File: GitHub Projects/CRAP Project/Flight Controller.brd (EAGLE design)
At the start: 40 x 93 mm, 126 parts, among them J1 2POS_SCREWTERM, J101 2POS_SCREWTERM, J2 4POS_SCREWTERM, J3 4POS_SCREWTERM, J4 4POS_SCREWTERM, J5 4POS_SCREWTERM, Q101 IPD042P03L3G, Q102 IPD042P03L3G, Q1101 PMF170XP, Q1102 DMG4800LSD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

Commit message: Routing, schematic changes
1. Changed some schematic errors on the firing chains
2. Routed more GPS, changed inductor on power supply, routed Xbee
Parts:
- L801, L802: device rcl:L1812 -> rcl:R0805
- moved C805 499.3 mm to (30.0, 97.0)
- moved L804 499.3 mm to (12.0, 102.0)
- moved L803 494.5 mm to (23.0, 96.0), turned to 180 degrees
- moved L801 480.2 mm to (30.0, 89.0), turned to 270 degrees
- moved L802 476.2 mm to (10.0, 89.0), turned to 270 degrees
- moved C803 469.5 mm to (29.0, 81.0), turned to 90 degrees
- moved C804 469.5 mm to (29.0, 77.0), turned to 90 degrees
- moved C802 467.5 mm to (26.0, 84.0), turned to 315 degrees
- moved C801 460.8 mm to (15.0, 85.0)
- moved J5 197.6 mm to (34.0, 39.5), turned to 90 degrees
- moved C2 175.6 mm to (21.0, 44.0), flipped to the bottom, turned to 135 degrees
- moved C1 172.2 mm to (19.0, 46.0), flipped to the bottom, turned to 45 degrees
- moved C3 167.8 mm to (17.6, 49.1), flipped to the bottom, turned to 135 degrees
- moved L101 4.12 mm to (27.0, 40.0), flipped to the bottom
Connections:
- removed net FC2+: J3.3
- removed net FC4+: J4.3
- removed net GPS1:+3V3: C803.2, C804.2, U$801.8
- net +12V: now also J3.3, J4.3
- net +3V3: now also C803.2, C804.2, U$801.8
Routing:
- net +3V3: track 75.0 -> 252.1 mm, vias 4 -> 8
- net VDDOUT: track 0.00 -> 24.9 mm, vias 0 -> 3
- net GPS1:N$2: track 0.00 -> 17.7 mm, vias 0 -> 1
- net GPS1:N$3: track 0.00 -> 12.6 mm, vias 0 -> 1
- net DCDC_REGULATOR:N$3: track 6.94 -> 9.19 mm, vias 0 -> 1
- net DCDC_REGULATOR:N$5: track 13.2 -> 14.7 mm, vias 0 -> 1
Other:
- board text added: "BW_1"
- board text added: "BW_2"

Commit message: More routing changes
1. Changed the power circuit 180 degrees to better fit the inductor
2. Routed a lot of the ordance circuits and placed all MOSFETS
3. Routed lots of power
4. Oh god it's so crowded
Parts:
- moved Q1102 402.9 mm to (28.6, 68.1), flipped to the bottom, turned to 180 degrees
- moved Q1202 342.6 mm to (27.0, 60.0), flipped to the bottom, turned to 90 degrees
- moved Q1302 287.1 mm to (27.0, 54.0), flipped to the bottom, turned to 90 degrees
- moved C307 263.2 mm to (10.2, 54.9), flipped to the bottom, turned to 270 degrees
- moved C306 261.8 mm to (9.22, 60.0), flipped to the bottom, turned to 270 degrees
- moved U301 130.2 mm to (4.61, 59.3), flipped to the bottom
- moved D301 120.1 mm to (18.3, 72.3), flipped to the bottom
- moved L101 18.1 mm to (9.00, 38.0), flipped to the top
- moved C103 9.79 mm to (23.7, 35.5), turned to 180 degrees
- moved U$101 9.00 mm to (15.0, 33.0), turned to 180 degrees
- moved C102 7.64 mm to (23.2, 32.3), turned to 90 degrees
- moved C804 3.36 mm to (28.5, 80.3), turned to 0 degrees
- moved R102 3.30 mm to (16.8, 63.8)
- moved R106 3.27 mm to (20.9, 32.2), turned to 270 degrees
- moved C101 2.22 mm to (18.7, 32.2), turned to 90 degrees
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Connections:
- removed net FC3-: J4.2
- net FC1-2: now also J4.2
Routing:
- net DCDC_REGULATOR:VIN: track 18.9 -> 72.1 mm
- net ORDNANCE_POWER:N$3: track 0.00 -> 28.6 mm, vias 0 -> 1
- net ORDNANCE_POWER:N$7: track 0.00 -> 11.1 mm
- net FC1-3: track 0.00 -> 10.5 mm
- net DCDC_REGULATOR:N$5: track 14.7 -> 6.54 mm, vias 1 -> 0
- net FC1-2: track 0.00 -> 7.50 mm
- net FC1-1: track 0.00 -> 7.35 mm
- net VCC_IN: track 29.9 -> 25.9 mm
- net DCDC_REGULATOR:N$3: track 9.19 -> 12.7 mm, vias 1 -> 0
- net DCDC_REGULATOR:N$6: track 35.8 -> 39.1 mm, vias 0 -> 2
- net FC1-: track 4.80 -> 7.73 mm
- net +3V3: track 252.1 -> 254.0 mm
- net DCDC_REGULATOR:N$2: track 22.8 -> 21.3 mm
- net DCDC_REGULATOR:N$4: track 9.78 -> 11.1 mm
- net DCDC_REGULATOR:N$11: track 8.65 -> 7.93 mm
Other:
- board size 40 x 93 mm -> 40 x 95 mm

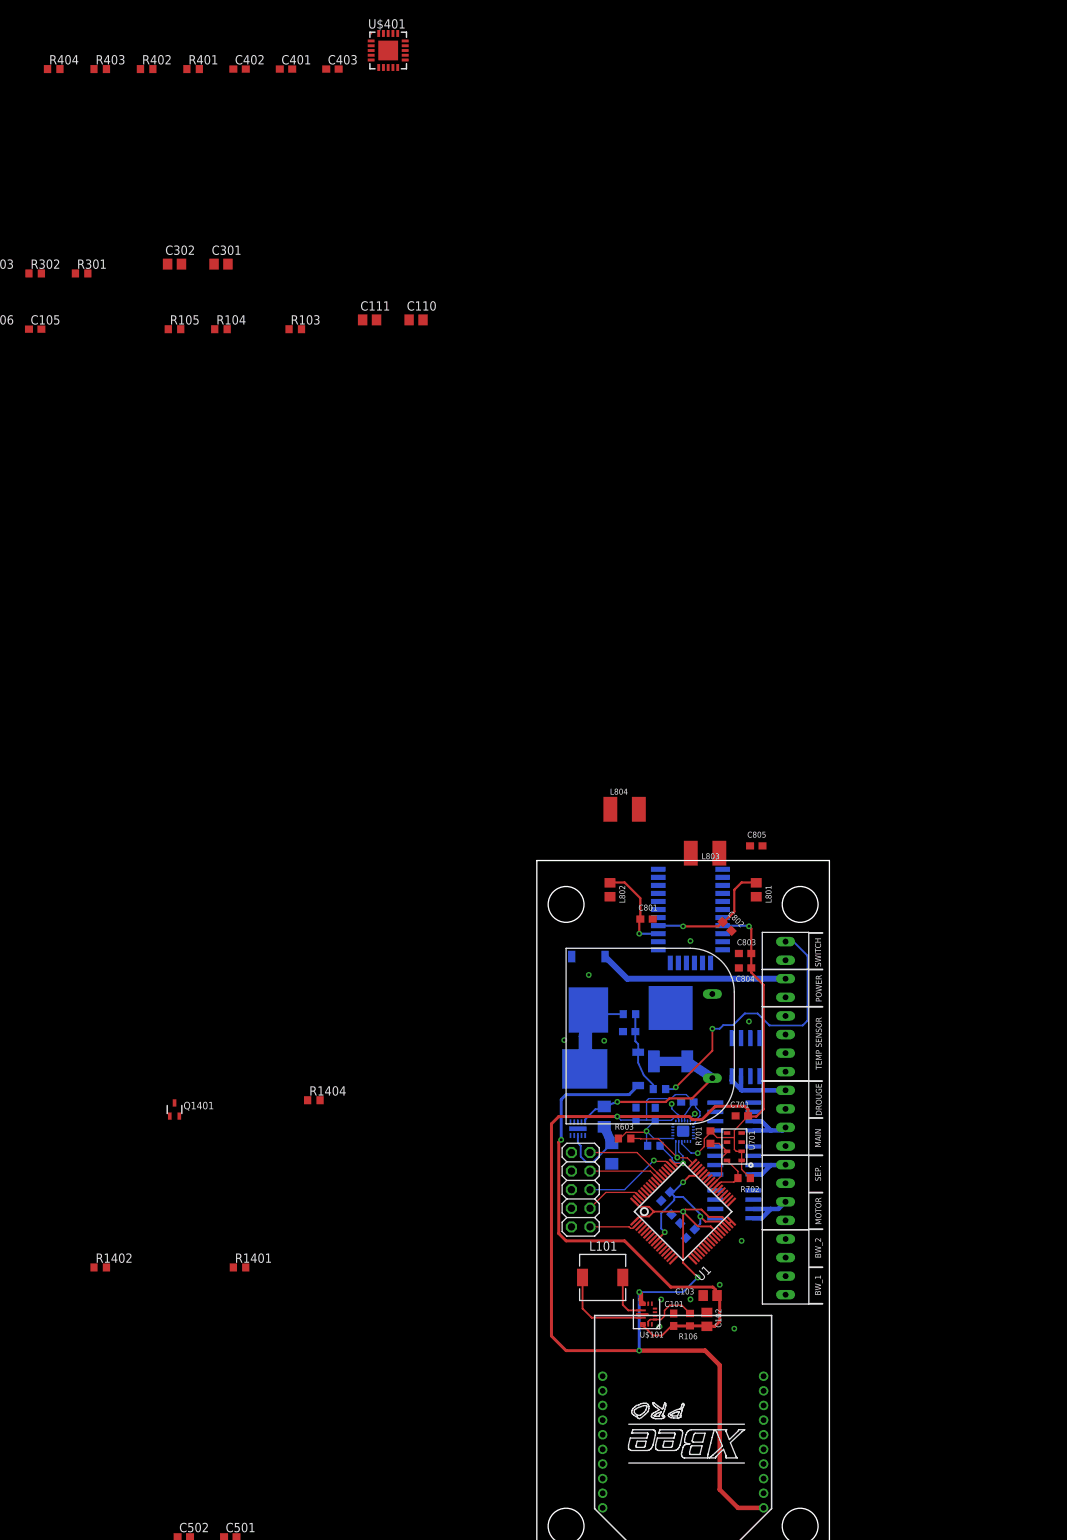
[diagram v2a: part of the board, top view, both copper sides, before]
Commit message: More routing
1. Routed parts of the ordance
2. Routed parts of the RTD
3. Routed Parts of the breakwire
4. Swapped RTD and breakwire headers to allow for actual routing because
it was too cramped to fit the RTD's sensor chip in the area that the
header was in
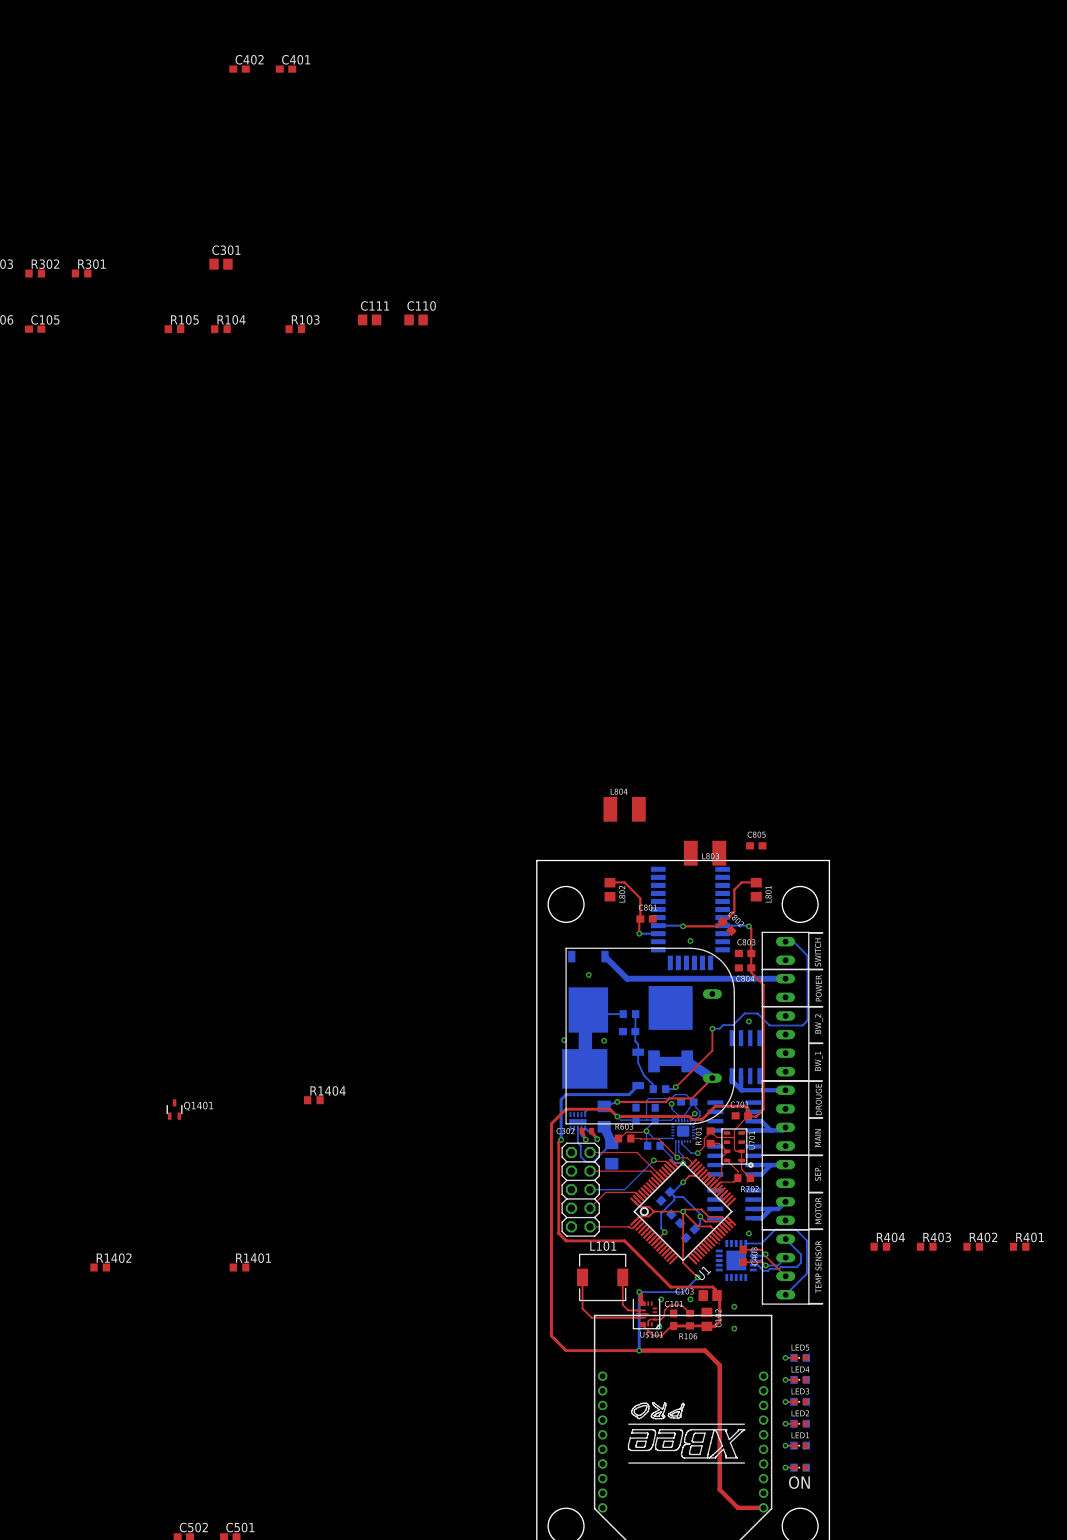
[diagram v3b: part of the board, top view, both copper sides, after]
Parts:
- added LED1, LED2, LED3, LED4, LED5, ON: (no value), led:CHIPLED_0603
- added R3, R4, R5, R6, R7, R8: (no value), rcl:R0603
- C302: device rcl:C0805 -> rcl:C0402
- moved R401 196.7 mm to (66.0, 42.2)
- moved R402 196.7 mm to (59.7, 42.2)
- moved R403 196.7 mm to (53.3, 42.2)
- moved R404 196.7 mm to (47.0, 42.2)
- moved U$401 172.1 mm to (27.3, 40.3), flipped to the bottom, turned to 270 degrees
- moved C403 171.7 mm to (28.2, 40.9), turned to 270 degrees
- moved C302 131.2 mm to (6.83, 58.0), turned to 180 degrees
- moved J2 30.5 mm to (34.0, 39.4)
- moved J5 30.5 mm to (34.0, 69.9)
- moved U301 1.00 mm to (4.61, 60.3)
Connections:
- new net N$24: LED1.C, R4.2
- new net N$25: LED2.C, R5.2
- new net N$26: LED3.C, R6.2
- new net N$27: LED4.C, R7.2
- new net N$28: LED5.C, R8.2
- new net N$30: ON.C, R3.2
- new net UC_LED1: LED1.A
- new net UC_LED2: LED2.A
- new net UC_LED3: LED3.A
- new net UC_LED4: LED4.A
- new net UC_LED5: LED5.A
- net +3V3: now also ON.A
- net GND: now also R3.1, R4.1, R5.1, R6.1, R7.1, R8.1
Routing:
- net N$6: track 0.00 -> 18.4 mm
- net N$9: track 0.00 -> 11.4 mm
- net N$7: track 0.00 -> 9.27 mm, vias 0 -> 1
- net N$8: track 0.00 -> 8.45 mm, vias 0 -> 1
- net ORDNANCE_POWER:N$1: track 0.00 -> 3.59 mm, vias 0 -> 1
- net ORDNANCE_POWER:N$2: track 0.00 -> 3.09 mm, vias 0 -> 1
- net N$30: track 0.00 -> 2.40 mm, vias 0 -> 1
- net N$28: track 0.00 -> 2.40 mm, vias 0 -> 1
- net N$27: track 0.00 -> 2.40 mm, vias 0 -> 1
- net N$26: track 0.00 -> 2.40 mm, vias 0 -> 1
- net N$25: track 0.00 -> 2.40 mm, vias 0 -> 1
- net N$24: track 0.00 -> 2.40 mm, vias 0 -> 1
- net ORDNANCE_POWER:N$7: track 11.1 -> 12.1 mm
- net +3V3: track 254.0 -> 254.8 mm

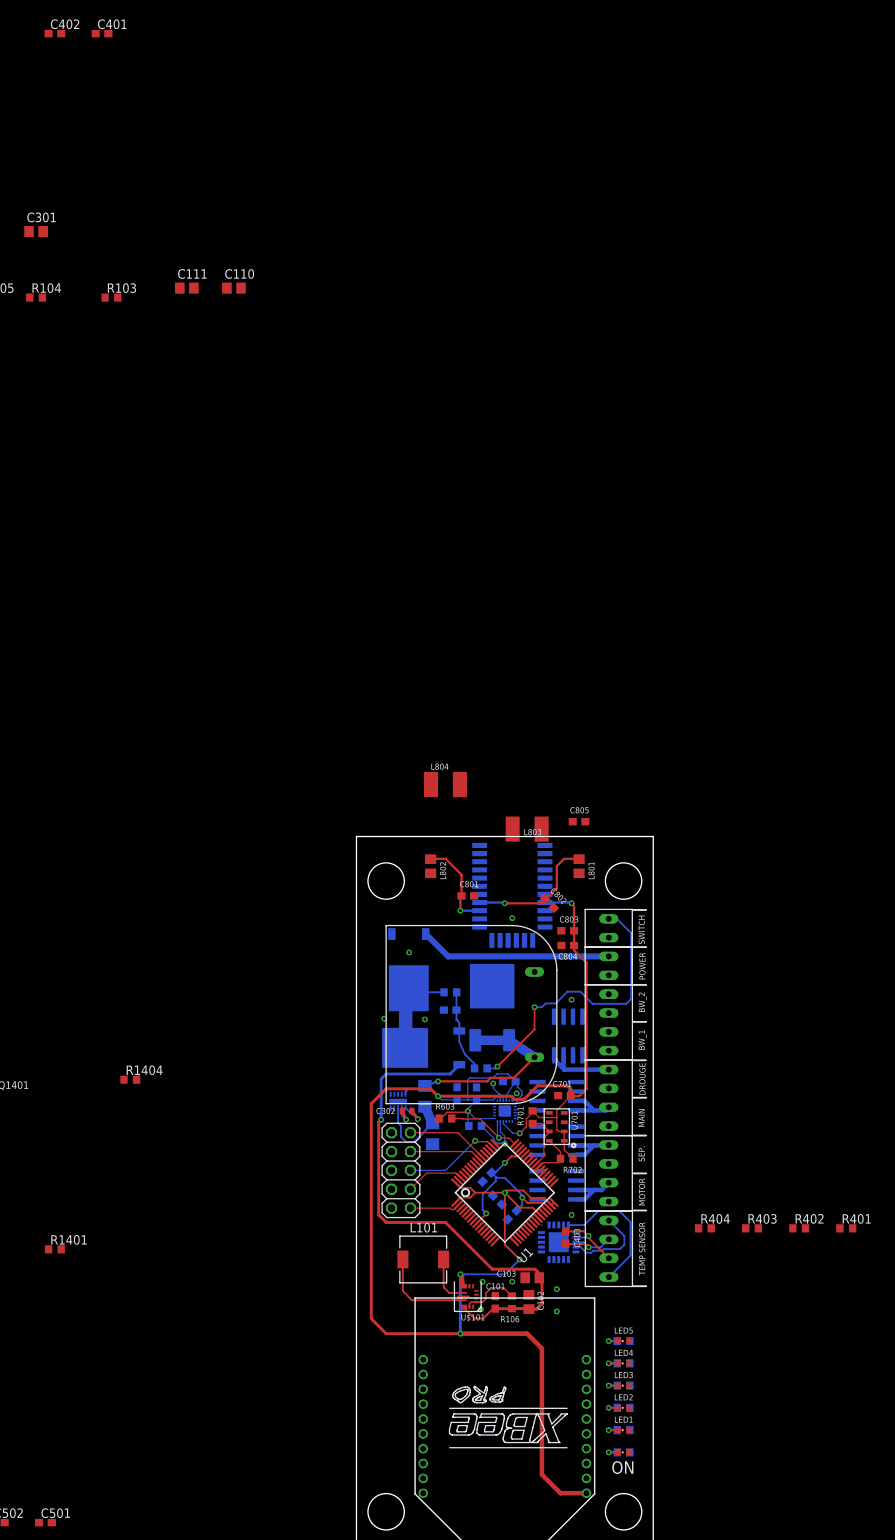
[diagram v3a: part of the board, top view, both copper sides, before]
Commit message: Routed some of the RTD sensor
Moved the RTD chip under the Xbee to have more room for capacitors and
resistors later on
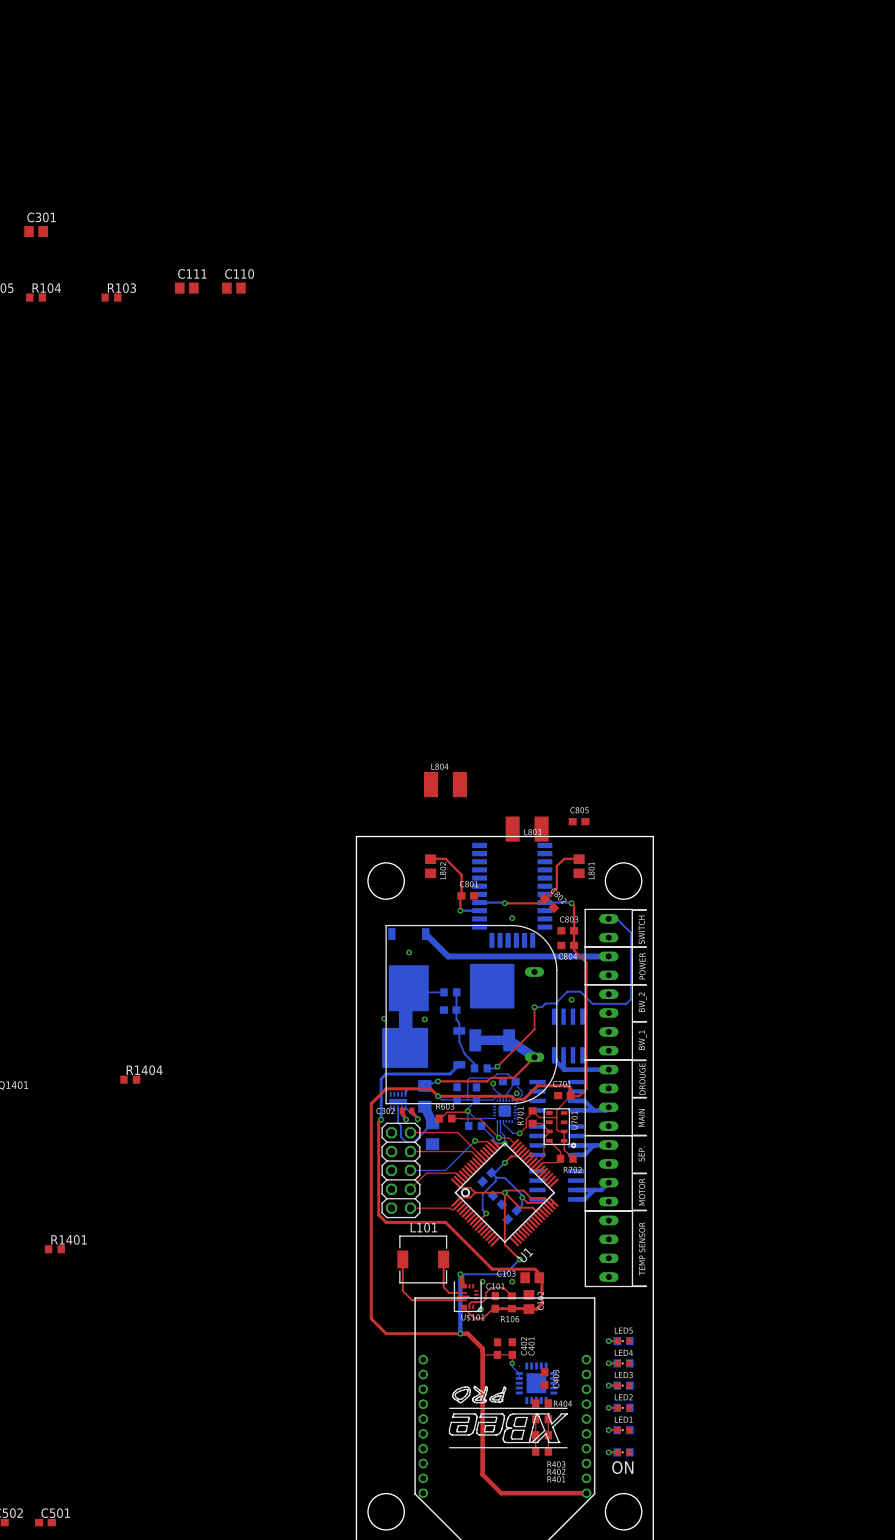
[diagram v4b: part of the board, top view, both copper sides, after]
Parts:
- moved C402 187.0 mm to (19.0, 26.0), turned to 90 degrees
- moved C401 185.6 mm to (21.0, 26.0), turned to 90 degrees
- moved R401 50.9 mm to (25.0, 12.1), turned to 180 degrees
- moved R402 44.5 mm to (25.0, 14.3), turned to 180 degrees
- moved R403 38.2 mm to (25.0, 16.5), turned to 180 degrees
- moved R404 32.2 mm to (25.0, 18.6), turned to 180 degrees
- moved U$401 19.2 mm to (24.3, 21.3)
- moved C403 19.2 mm to (25.4, 21.9)
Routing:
- net N$6: track 18.4 -> 0.00 mm
- net N$9: track 11.4 -> 0.00 mm
- net N$7: track 9.27 -> 0.00 mm, vias 1 -> 0
- net N$8: track 8.45 -> 0.00 mm, vias 1 -> 0
- net +3V3: track 254.8 -> 262.8 mm, vias 8 -> 9
- net RTD:N$1: track 0.00 -> 4.37 mm
- net RTD:N$4: track 0.00 -> 4.37 mm
